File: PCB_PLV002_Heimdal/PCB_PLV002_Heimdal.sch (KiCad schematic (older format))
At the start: 8 parts

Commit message: Work on Heimdal and Yggdrasil
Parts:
- C8: renamed from C?; footprint (none) -> Capacitor_SMD:C_0603_1608Metric_Pad1.05x0.95mm_HandSolder
- R13: renamed from R?; value R_US -> 120; footprint (none) -> Resistor_SMD:R_0603_1608Metric_Pad1.05x0.95mm_HandSolder
- gave numbers to parts that had none: 6
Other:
- note added: "Acquistion"
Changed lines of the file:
@@
 EESchema Schematic File Version 4
+LIBS:PCB_PLV002_Heimdal-cache
 EELAYER 29 0
 EELAYER END
 $Descr USLetter 11000 8500
 encoding utf-8
-Sheet 1 2
+Sheet 1 3
 Title "Heimdal Sensor Interface Board"
 Date ""
@@
 QuantumBeat
 $Comp
-L boringlib:NUCLEO-L476RG NCLO?
+L boringlib:NUCLEO-L476RG NCLO1
 U 1 1 5FB4B31E
 P 3250 5600
-F 0 "NCLO?" H 1700 7650 50  0000 C CNN
+F 0 "NCLO1" H 1700 7650 50  0000 C CNN
 F 1 "NUCLEO-L476RG" H 1900 3650 50  0000 C CNN
 F 2 "BoringFootprints:ST_Nucleo-64" H 3200 4900 50  0001 C CNN
@@
 $EndComp
 $Comp
-L Interface_CAN_LIN:SN65HVD232 U?
+L Interface_CAN_LIN:SN65HVD232 U7
 U 1 1 5FB5123E
 P 7400 5300
-F 0 "U?" H 7150 5550 50  0000 C CNN
+F 0 "U7" H 7150 5550 50  0000 C CNN
 F 1 "SN65HVD232" H 7050 4950 50  0000 C CNN
 F 2 "Package_SO:SOIC-8_3.9x4.9mm_P1.27mm" H 7400 4800 50  0001 C CNN
@@
 	6700 5300 7000 5300
 $Comp
-L Device:R_US R?
+L Device:R_US R13
 U 1 1 5FB52878
 P 8250 5300
-F 0 "R?" V 8045 5300 50  0000 C CNN
-F 1 "R_US" V 8136 5300 50  0000 C CNN
-F 2 "" V 8290 5290 50  0001 C CNN
+F 0 "R13" V 8045 5300 50  0000 C CNN
+F 1 "120" V 8136 5300 50  0000 C CNN
+F 2 "Resistor_SMD:R_0603_1608Metric_Pad1.05x0.95mm_HandSolder" V 8290 5290 50  0001 C CNN
 F 3 "~" H 8250 5300 50  0001 C CNN
 	1    8250 5300
@@
 $EndComp
 $Comp
-L Device:Jumper_NC_Small JP?
+L Device:Jumper_NC_Small JP1
 U 1 1 5FB538A6
 P 8600 5300
-F 0 "JP?" H 8600 5512 50  0000 C CNN
+F 0 "JP1" H 8600 5512 50  0000 C CNN
 F 1 "CAN_TERM" H 8600 5421 50  0000 C CNN
 F 2 "" H 8600 5300 50  0001 C CNN
@@
 CANL
 $Comp
-L power:+3.3V #PWR?
+L power:+3.3V #PWR0101
 U 1 1 5FB56159
 P 7400 4950
-F 0 "#PWR?" H 7400 4800 50  0001 C CNN
+F 0 "#PWR0101" H 7400 4800 50  0001 C CNN
 F 1 "+3.3V" H 7415 5123 50  0000 C CNN
 F 2 "" H 7400 4950 50  0001 C CNN
@@
 	7400 5700 7400 5750
 $Comp
-L power:GND #PWR?
+L power:GND #PWR0102
 U 1 1 5FB56C50
 P 7400 5750
-F 0 "#PWR?" H 7400 5500 50  0001 C CNN
+F 0 "#PWR0102" H 7400 5500 50  0001 C CNN
 F 1 "GND" H 7405 5577 50  0000 C CNN
 F 2 "" H 7400 5750 50  0001 C CNN
@@
 $EndComp
 $Comp
-L power:+3.3V #PWR?
+L power:+3.3V #PWR0103
 U 1 1 5FB575C6
 P 9000 5100
-F 0 "#PWR?" H 9000 4950 50  0001 C CNN
+F 0 "#PWR0103" H 9000 4950 50  0001 C CNN
 F 1 "+3.3V" H 9015 5273 50  0000 C CNN
 F 2 "" H 9000 5100 50  0001 C CNN
@@
 $EndComp
 $Comp
-L power:GND #PWR?
+L power:GND #PWR0104
 U 1 1 5FB57C14
 P 9000 5500
-F 0 "#PWR?" H 9000 5250 50  0001 C CNN
+F 0 "#PWR0104" H 9000 5250 50  0001 C CNN
 F 1 "GND" H 9005 5327 50  0000 C CNN
 F 2 "" H 9000 5500 50  0001 C CNN
@@
 $EndComp
 $Comp
-L Device:C C?
+L Device:C C8
 U 1 1 5FB58397
 P 9000 5300
-F 0 "C?" H 9115 5346 50  0000 L CNN
+F 0 "C8" H 9115 5346 50  0000 L CNN
 F 1 "0.1uF" H 9115 5255 50  0000 L CNN
-F 2 "" H 9038 5150 50  0001 C CNN
+F 2 "Capacitor_SMD:C_0603_1608Metric_Pad1.05x0.95mm_HandSolder" H 9038 5150 50  0001 C CNN
 F 3 "~" H 9000 5300 50  0001 C CNN
 	1    9000 5300
@@
 Using Nucleo 5V and 3.3V regulation\nMax current 800mA on 5V?\n500mA on 3.3V
 $Comp
-L power:+12V #PWR?
+L power:+12V #PWR0105
 U 1 1 5FB5A7AA
 P 3750 3450
-F 0 "#PWR?" H 3750 3300 50  0001 C CNN
+F 0 "#PWR0105" H 3750 3300 50  0001 C CNN
 F 1 "+12V" H 3765 3623 50  0000 C CNN
 F 2 "" H 3750 3450 50  0001 C CNN
@@
 	2850 3450 2850 3500
 $Comp
-L power:+5V #PWR?
+L power:+5V #PWR0106
 U 1 1 5FB5BBCE
 P 2850 3450
-F 0 "#PWR?" H 2850 3300 50  0001 C CNN
+F 0 "#PWR0106" H 2850 3300 50  0001 C CNN
 F 1 "+5V" H 2865 3623 50  0000 C CNN
 F 2 "" H 2850 3450 50  0001 C CNN
@@
 $EndComp
 $Comp
-L power:+3.3V #PWR?
+L power:+3.3V #PWR0107
 U 1 1 5FB5C656
 P 3150 3450
-F 0 "#PWR?" H 3150 3300 50  0001 C CNN
+F 0 "#PWR0107" H 3150 3300 50  0001 C CNN
 F 1 "+3.3V" H 3165 3623 50  0000 C CNN
 F 2 "" H 3150 3450 50  0001 C CNN
@@
 CAN_TX
 $Comp
-L Connector_Generic:Conn_01x12 J?
+L Connector_Generic:Conn_01x12 J1
 U 1 1 5FB5EF88
 P 1000 1550
-F 0 "J?" H 918 725 50  0000 C CNN
+F 0 "J1" H 918 725 50  0000 C CNN
 F 1 "Conn_01x12" H 918 816 50  0000 C CNN
 F 2 "" H 1000 1550 50  0001 C CNN
@@
 NoConn ~ 1200 950
 $Comp
-L power:GND #PWR?
+L power:GND #PWR0108
 U 1 1 5FB625D6
 P 1250 2100
-F 0 "#PWR?" H 1250 1850 50  0001 C CNN
+F 0 "#PWR0108" H 1250 1850 50  0001 C CNN
 F 1 "GND" H 1255 1927 50  0000 C CNN
 F 2 "" H 1250 2100 50  0001 C CNN
@@
 Connection ~ 1600 1750
 $Comp
-L Device:Fuse F?
+L Device:Fuse F1
 U 1 1 5FB68FE4
 P 1800 1750
-F 0 "F?" V 1603 1750 50  0000 C CNN
+F 0 "F1" V 1603 1750 50  0000 C CNN
 F 1 "Fuse" V 1694 1750 50  0000 C CNN
 F 2 "" V 1730 1750 50  0001 C CNN
@@
 $EndComp
 $Comp
-L Device:D_Schottky D?
+L Device:D_Schottky D1
 U 1 1 5FB699D0
 P 2150 1750
-F 0 "D?" H 2150 1534 50  0000 C CNN
+F 0 "D1" H 2150 1534 50  0000 C CNN
 F 1 "D_Schottky" H 2150 1625 50  0000 C CNN
 F 2 "" H 2150 1750 50  0001 C CNN
@@
 	2450 1750 2450 1700
 $Comp
-L power:+24V #PWR?
+L power:+24V #PWR0109
 U 1 1 5FB6B6D5
 P 2450 1700
-F 0 "#PWR?" H 2450 1550 50  0001 C CNN
+F 0 "#PWR0109" H 2450 1550 50  0001 C CNN
 F 1 "+24V" H 2465 1873 50  0000 C CNN
 F 2 "" H 2450 1700 50  0001 C CNN
@@
 	750  4000 1450 4000
 $Comp
-L power:GND #PWR?
+L power:GND #PWR0110
 U 1 1 5FB71819
 P 3650 7800
-F 0 "#PWR?" H 3650 7550 50  0001 C CNN
+F 0 "#PWR0110" H 3650 7550 50  0001 C CNN
 F 1 "GND" H 3655 7627 50  0000 C CNN
 F 2 "" H 3650 7800 50  0001 C CNN
@@
 Wire Wire Line
 	6650 1600 7450 1600
+$Sheet
+S 7450 2150 1900 1150
+U 5FBDDE45
+F0 "Acquisition" 50
+F1 "Acquisition.sch" 50
+$EndSheet
+Text Notes 7950 3250 0    118  ~ 0
+Acquistion
 $EndSCHEMATC

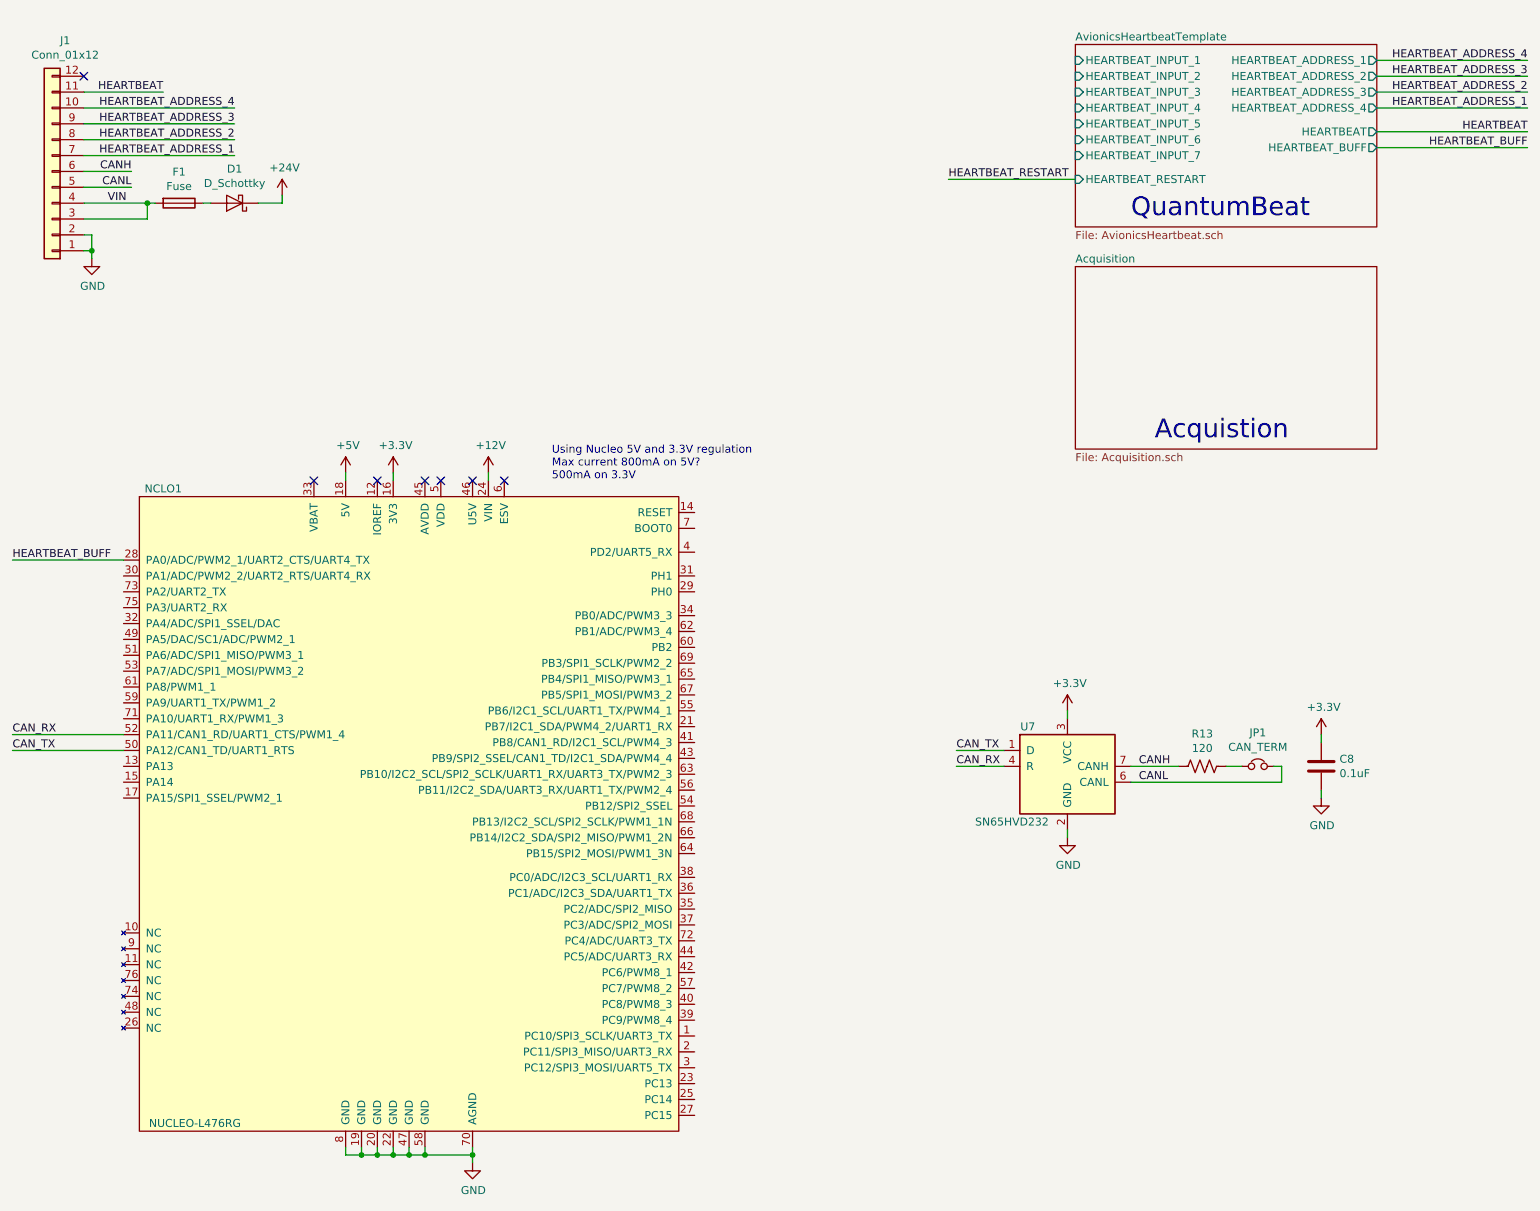
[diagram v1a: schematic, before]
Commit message: Most of sensors for heimdal complete, still need to sort out load cells, flammable gas
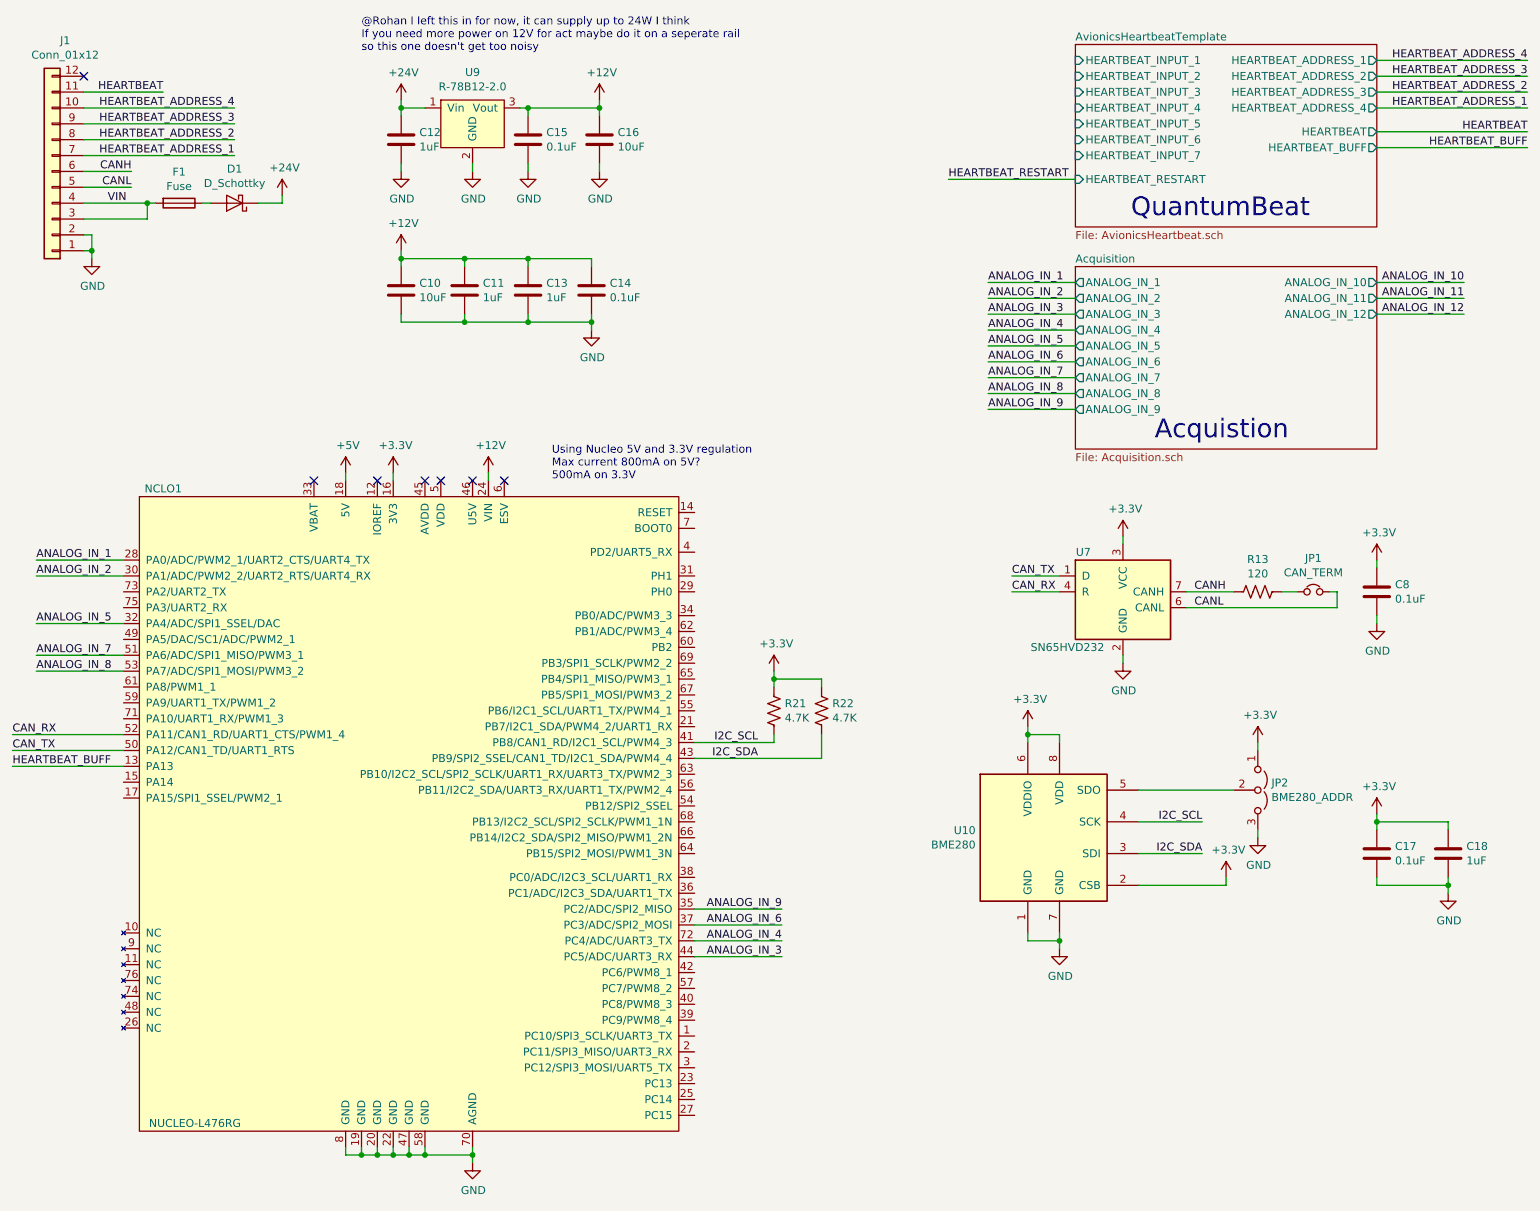
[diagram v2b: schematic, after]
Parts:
- added C10, C16: 10uF, Capacitor_SMD:C_0603_1608Metric_Pad1.05x0.95mm_HandSolder, symbol Device:C
- added C11, C12, C13, C18: 1uF, Capacitor_SMD:C_0603_1608Metric_Pad1.05x0.95mm_HandSolder, symbol Device:C
- added C14, C15, C17: 0.1uF, Capacitor_SMD:C_0603_1608Metric_Pad1.05x0.95mm_HandSolder, symbol Device:C
- added JP2: BME280_ADDR, symbol Jumper:Jumper_3_Open
- added R21, R22: 4.7K, Resistor_SMD:R_0603_1608Metric_Pad1.05x0.95mm_HandSolder, symbol Device:R_US
- added U10: BME280, Package_LGA:Bosch_LGA-8_2.5x2.5mm_P0.65mm_ClockwisePinNumbering, symbol Sensor:BME280
- added U9: R-78B12-2.0, Converter_DCDC:Converter_DCDC_RECOM_R-78B-2.0_THT, symbol boringlib:R-78B12-2.0
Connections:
- net +12V: now also C10.1, C11.1, C13.1, C14.1, C15.1, C16.1, U9.3 (Vout)
- net +24V: now also C12.1, U9.1 (Vin)
- net +3V3: now also C17.1, C18.1, JP2.1 (A), R21.1, R22.1, U10.2 (CSB), U10.6 (VDDIO), U10.8 (VDD)
- net GND: now also C10.2, C11.2, C12.2, C13.2, C14.2, C15.2, C16.2, C17.2, C18.2, JP2.3 (B), U10.1 (GND), U10.7 (GND), U9.2 (GND)
- net HEARTBEAT_BUFF: now also NCLO1.13 (PA13); no longer NCLO1.28 (PA0/ADC/PWM2_1/UART2_CTS/UART4_TX)
- net ANALOG_IN_2: now reaches NCLO1.30 (PA1/ADC/PWM2_2/UART2_RTS/UART4_RX)
- net ANALOG_IN_5: now reaches NCLO1.32 (PA4/ADC/SPI1_SSEL/DAC)
- net ANALOG_IN_9: now reaches NCLO1.35 (PC2/ADC/SPI2_MISO)
- net ANALOG_IN_6: now reaches NCLO1.37 (PC3/ADC/SPI2_MOSI)
- net I2C_SCL: now reaches NCLO1.41 (PB8/CAN1_RD/I2C1_SCL/PWM4_3)
- net I2C_SCL: now also R21.2, U10.4 (SCK)
- net I2C_SDA: now reaches NCLO1.43 (PB9/SPI2_SSEL/CAN1_TD/I2C1_SDA/PWM4_4)
- net I2C_SDA: now also R22.2, U10.3 (SDI)
- net ANALOG_IN_3: now reaches NCLO1.44 (PC5/ADC/UART3_RX)
- net ANALOG_IN_7: now reaches NCLO1.51 (PA6/ADC/SPI1_MISO/PWM3_1)
- net ANALOG_IN_8: now reaches NCLO1.53 (PA7/ADC/SPI1_MOSI/PWM3_2)
- net ANALOG_IN_4: now reaches NCLO1.72 (PC4/ADC/UART3_TX)
- new net: JP2.2 (C), U10.5 (SDO)
- new net ANALOG_IN_1: NCLO1.28 (PA0/ADC/PWM2_1/UART2_CTS/UART4_TX)
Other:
- note added: "@Rohan I left this in for now, it can supply up to 24W I think\nIf you need more power on 12V for act maybe do it on a seperate rail\nso this one doesn't get too noisy"
- moved on the sheet: C8, JP1, R13, U7
